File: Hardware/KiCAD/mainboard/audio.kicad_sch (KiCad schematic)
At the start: 16 parts, among them IC1 LM4861M

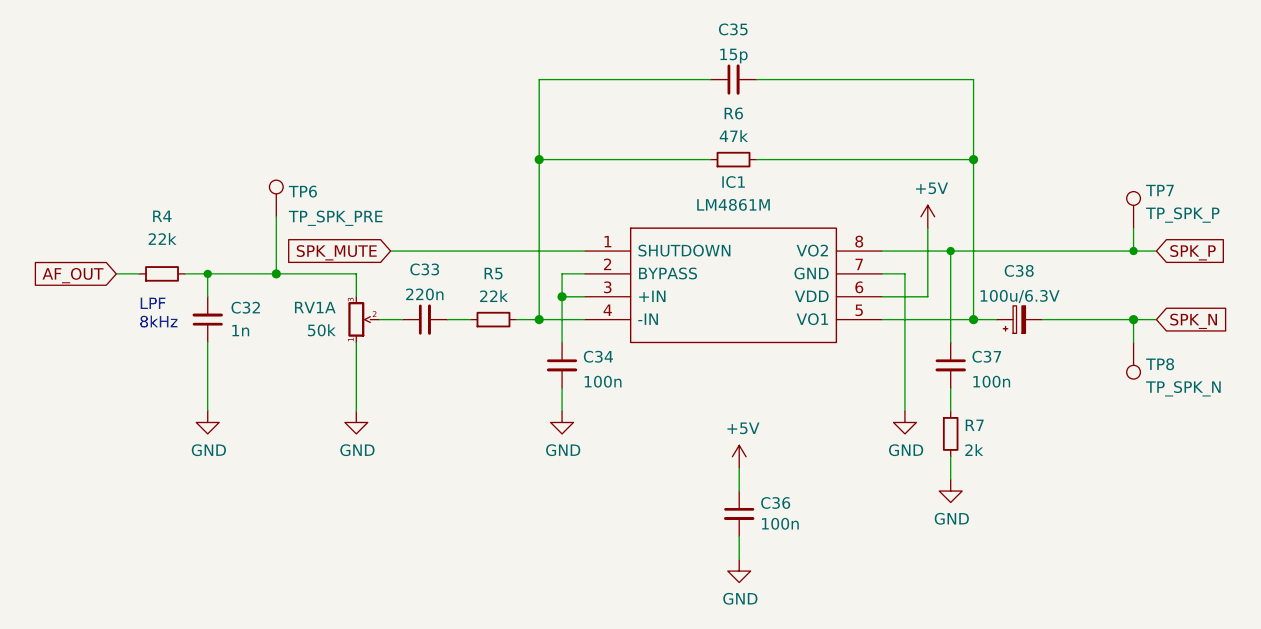
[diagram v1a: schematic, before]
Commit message: MCU swap
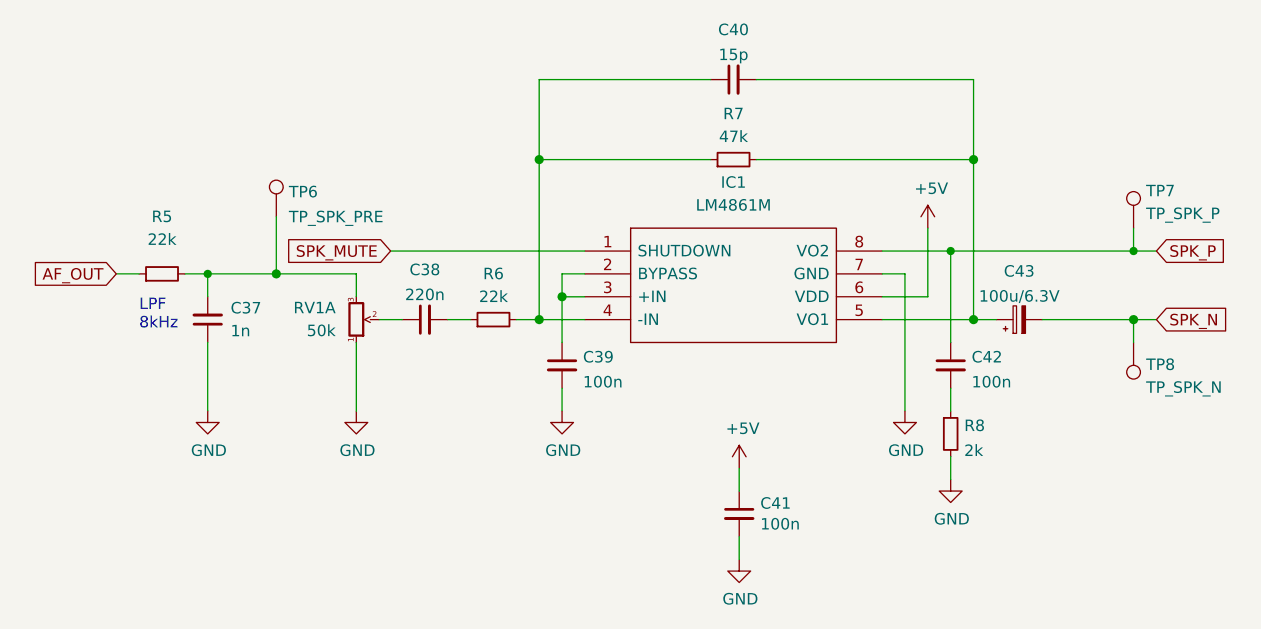
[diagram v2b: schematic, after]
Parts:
- renumbered C32 to C37, C33 to C38, C34 to C39, C35 to C40, C36 to C41, C37 to C42, C38 to C43, R4 to R5, R5 to R6, R6 to R7, R7 to R8
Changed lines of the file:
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@@
   (symbol (lib_id "pkl_device:pkl_R_Small") (at 146.05 84.455 90) (unit 1)
     (in_bom yes) (on_board yes)
-    (property "Reference" "R6" (id 0) (at 146.05 79.375 90))
+    (property "Reference" "R7" (id 0) (at 146.05 79.375 90))
     (property "Value" "47k" (id 1) (at 146.05 81.915 90))
     (property "Footprint" "Resistor_SMD:R_0402_1005Metric" (id 2) (at 146.05 84.455 0)
@@
   (symbol (lib_id "pkl_device:pkl_C_Small") (at 170.18 107.315 0) (unit 1)
     (in_bom yes) (on_board yes) (fields_autoplaced)
-    (property "Reference" "C37" (id 0) (at 172.5042 106.4065 0)
+    (property "Reference" "C42" (id 0) (at 172.5042 106.4065 0)
       (effects (font (size 1.27 1.27)) (justify left))
     )
@@
   (symbol (lib_id "pkl_device:pkl_C_Small") (at 87.63 102.235 180) (unit 1)
     (in_bom yes) (on_board yes) (fields_autoplaced)
-    (property "Reference" "C32" (id 0) (at 90.17 100.9585 0)
+    (property "Reference" "C37" (id 0) (at 90.17 100.9585 0)
       (effects (font (size 1.27 1.27)) (justify right))
     )
@@
   (symbol (lib_id "pkl_device:pkl_C_Small") (at 127 107.315 0) (unit 1)
     (in_bom yes) (on_board yes) (fields_autoplaced)
-    (property "Reference" "C34" (id 0) (at 129.3242 106.4065 0)
+    (property "Reference" "C39" (id 0) (at 129.3242 106.4065 0)
       (effects (font (size 1.27 1.27)) (justify left))
     )
@@
   (symbol (lib_id "pkl_device:pkl_R_Small") (at 119.38 102.235 90) (unit 1)
     (in_bom yes) (on_board yes)
-    (property "Reference" "R5" (id 0) (at 119.38 97.155 90))
+    (property "Reference" "R6" (id 0) (at 119.38 97.155 90))
     (property "Value" "22k" (id 1) (at 119.38 99.695 90))
     (property "Footprint" "Resistor_SMD:R_0402_1005Metric" (id 2) (at 119.38 102.235 0)
@@
   (symbol (lib_id "power:+5V") (at 146.685 118.745 0) (unit 1)
     (in_bom yes) (on_board yes)
-    (property "Reference" "#PWR044" (id 0) (at 146.685 122.555 0)
+    (property "Reference" "#PWR052" (id 0) (at 146.685 122.555 0)
       (effects (font (size 1.27 1.27)) hide)
     )
@@
   (symbol (lib_id "pkl_device:pkl_C_Small") (at 111.76 102.235 90) (unit 1)
     (in_bom yes) (on_board yes) (fields_autoplaced)
-    (property "Reference" "C33" (id 0) (at 111.76 96.7063 90))
+    (property "Reference" "C38" (id 0) (at 111.76 96.7063 90))
     (property "Value" "220n" (id 1) (at 111.76 99.4814 90))
     (property "Footprint" "Capacitor_SMD:C_0402_1005Metric" (id 2) (at 111.76 102.235 0)
@@
   (symbol (lib_id "pkl_device:pkl_C_Small") (at 146.685 123.825 0) (unit 1)
     (in_bom yes) (on_board yes)
-    (property "Reference" "C36" (id 0) (at 149.0218 122.6566 0)
+    (property "Reference" "C41" (id 0) (at 149.0218 122.6566 0)
       (effects (font (size 1.27 1.27)) (justify left))
     )
@@
   (symbol (lib_id "pkl_device:pkl_C_Small") (at 146.05 75.565 90) (unit 1)
     (in_bom yes) (on_board yes) (fields_autoplaced)
-    (property "Reference" "C35" (id 0) (at 146.05 70.0363 90))
+    (property "Reference" "C40" (id 0) (at 146.05 70.0363 90))
     (property "Value" "15p" (id 1) (at 146.05 72.8114 90))
     (property "Footprint" "Capacitor_SMD:C_0402_1005Metric" (id 2) (at 146.05 75.565 0)
@@
   (symbol (lib_id "pkl_device:pkl_R_Small") (at 82.55 97.155 90) (unit 1)
     (in_bom yes) (on_board yes) (fields_autoplaced)
-    (property "Reference" "R4" (id 0) (at 82.55 90.805 90))
+    (property "Reference" "R5" (id 0) (at 82.55 90.805 90))
     (property "Value" "22k" (id 1) (at 82.55 93.345 90))
     (property "Footprint" "Resistor_SMD:R_0402_1005Metric" (id 2) (at 82.55 97.155 0)
@@
   (symbol (lib_id "power:GND") (at 127 112.395 0) (unit 1)
     (in_bom yes) (on_board yes)
-    (property "Reference" "#PWR043" (id 0) (at 127 118.745 0)
+    (property "Reference" "#PWR051" (id 0) (at 127 118.745 0)
       (effects (font (size 1.27 1.27)) hide)
     )
@@
   (symbol (lib_id "power:+5V") (at 167.64 92.075 0) (unit 1)
     (in_bom yes) (on_board yes)
-    (property "Reference" "#PWR047" (id 0) (at 167.64 95.885 0)
+    (property "Reference" "#PWR055" (id 0) (at 167.64 95.885 0)
       (effects (font (size 1.27 1.27)) hide)
     )
@@
   (symbol (lib_id "power:GND") (at 170.18 120.015 0) (unit 1)
     (in_bom yes) (on_board yes)
-    (property "Reference" "#PWR048" (id 0) (at 170.18 126.365 0)
+    (property "Reference" "#PWR056" (id 0) (at 170.18 126.365 0)
       (effects (font (size 1.27 1.27)) hide)
     )
@@
   (symbol (lib_id "power:GND") (at 104.14 112.395 0) (unit 1)
     (in_bom yes) (on_board yes)
-    (property "Reference" "#PWR042" (id 0) (at 104.14 118.745 0)
+    (property "Reference" "#PWR050" (id 0) (at 104.14 118.745 0)
       (effects (font (size 1.27 1.27)) hide)
     )
@@
   (symbol (lib_id "pkl_device:pkl_CP_Small") (at 177.8 102.235 90) (unit 1)
     (in_bom yes) (on_board yes) (fields_autoplaced)
-    (property "Reference" "C38" (id 0) (at 177.8 96.8714 90))
+    (property "Reference" "C43" (id 0) (at 177.8 96.8714 90))
     (property "Value" "100u{slash}6.3V" (id 1) (at 177.8 99.6465 90))
     (property "Footprint" "Capacitor_SMD:C_1206_3216Metric" (id 2) (at 177.8 102.235 0)
@@
   (symbol (lib_id "power:GND") (at 165.1 112.395 0) (unit 1)
     (in_bom yes) (on_board yes)
-    (property "Reference" "#PWR046" (id 0) (at 165.1 118.745 0)
+    (property "Reference" "#PWR054" (id 0) (at 165.1 118.745 0)
       (effects (font (size 1.27 1.27)) hide)
     )
@@
   (symbol (lib_id "power:GND") (at 87.63 112.395 0) (unit 1)
     (in_bom yes) (on_board yes)
-    (property "Reference" "#PWR041" (id 0) (at 87.63 118.745 0)
+    (property "Reference" "#PWR049" (id 0) (at 87.63 118.745 0)
       (effects (font (size 1.27 1.27)) hide)
     )
@@
   (symbol (lib_id "pkl_device:pkl_R_Small") (at 170.18 114.935 0) (unit 1)
     (in_bom yes) (on_board yes) (fields_autoplaced)
-    (property "Reference" "R7" (id 0) (at 171.6787 114.0265 0)
+    (property "Reference" "R8" (id 0) (at 171.6787 114.0265 0)
       (effects (font (size 1.27 1.27)) (justify left))
     )
@@
   (symbol (lib_id "power:GND") (at 146.685 128.905 0) (unit 1)
     (in_bom yes) (on_board yes)
-    (property "Reference" "#PWR045" (id 0) (at 146.685 135.255 0)
-      (effects (font (size 1.27 1.27)) hide)
-    )
+    (property "Reference" "#PWR053" (id 0) (at 146.685 135.255 0)
+      (effects (font (size 1.27 1.27)) hide)
+    )

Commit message: Removed RTC
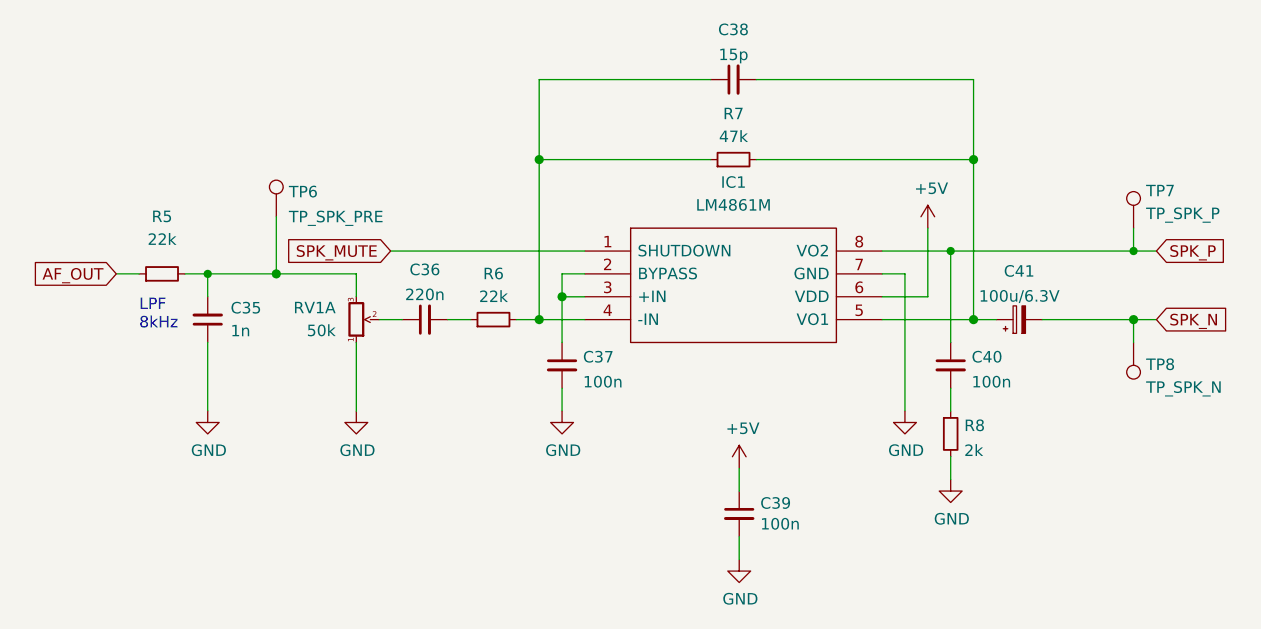
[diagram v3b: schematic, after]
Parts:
- renumbered C37 to C35, C38 to C36, C39 to C37, C40 to C38, C41 to C39, C42 to C40, C43 to C41
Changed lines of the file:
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@@
   (symbol (lib_id "pkl_device:pkl_C_Small") (at 170.18 107.315 0) (unit 1)
     (in_bom yes) (on_board yes) (fields_autoplaced)
-    (property "Reference" "C42" (id 0) (at 172.5042 106.4065 0)
+    (property "Reference" "C40" (id 0) (at 172.5042 106.4065 0)
       (effects (font (size 1.27 1.27)) (justify left))
     )
@@
   (symbol (lib_id "pkl_device:pkl_C_Small") (at 87.63 102.235 180) (unit 1)
     (in_bom yes) (on_board yes) (fields_autoplaced)
-    (property "Reference" "C37" (id 0) (at 90.17 100.9585 0)
+    (property "Reference" "C35" (id 0) (at 90.17 100.9585 0)
       (effects (font (size 1.27 1.27)) (justify right))
     )
@@
   (symbol (lib_id "pkl_device:pkl_C_Small") (at 127 107.315 0) (unit 1)
     (in_bom yes) (on_board yes) (fields_autoplaced)
-    (property "Reference" "C39" (id 0) (at 129.3242 106.4065 0)
+    (property "Reference" "C37" (id 0) (at 129.3242 106.4065 0)
       (effects (font (size 1.27 1.27)) (justify left))
     )
@@
   (symbol (lib_id "power:+5V") (at 146.685 118.745 0) (unit 1)
     (in_bom yes) (on_board yes)
-    (property "Reference" "#PWR052" (id 0) (at 146.685 122.555 0)
+    (property "Reference" "#PWR050" (id 0) (at 146.685 122.555 0)
       (effects (font (size 1.27 1.27)) hide)
     )
@@
   (symbol (lib_id "pkl_device:pkl_C_Small") (at 111.76 102.235 90) (unit 1)
     (in_bom yes) (on_board yes) (fields_autoplaced)
-    (property "Reference" "C38" (id 0) (at 111.76 96.7063 90))
+    (property "Reference" "C36" (id 0) (at 111.76 96.7063 90))
     (property "Value" "220n" (id 1) (at 111.76 99.4814 90))
     (property "Footprint" "Capacitor_SMD:C_0402_1005Metric" (id 2) (at 111.76 102.235 0)
@@
   (symbol (lib_id "pkl_device:pkl_C_Small") (at 146.685 123.825 0) (unit 1)
     (in_bom yes) (on_board yes)
-    (property "Reference" "C41" (id 0) (at 149.0218 122.6566 0)
+    (property "Reference" "C39" (id 0) (at 149.0218 122.6566 0)
       (effects (font (size 1.27 1.27)) (justify left))
     )
@@
   (symbol (lib_id "pkl_device:pkl_C_Small") (at 146.05 75.565 90) (unit 1)
     (in_bom yes) (on_board yes) (fields_autoplaced)
-    (property "Reference" "C40" (id 0) (at 146.05 70.0363 90))
+    (property "Reference" "C38" (id 0) (at 146.05 70.0363 90))
     (property "Value" "15p" (id 1) (at 146.05 72.8114 90))
     (property "Footprint" "Capacitor_SMD:C_0402_1005Metric" (id 2) (at 146.05 75.565 0)
@@
   (symbol (lib_id "power:GND") (at 127 112.395 0) (unit 1)
     (in_bom yes) (on_board yes)
-    (property "Reference" "#PWR051" (id 0) (at 127 118.745 0)
+    (property "Reference" "#PWR049" (id 0) (at 127 118.745 0)
       (effects (font (size 1.27 1.27)) hide)
     )
@@
   (symbol (lib_id "power:+5V") (at 167.64 92.075 0) (unit 1)
     (in_bom yes) (on_board yes)
-    (property "Reference" "#PWR055" (id 0) (at 167.64 95.885 0)
+    (property "Reference" "#PWR053" (id 0) (at 167.64 95.885 0)
       (effects (font (size 1.27 1.27)) hide)
     )
@@
   (symbol (lib_id "power:GND") (at 170.18 120.015 0) (unit 1)
     (in_bom yes) (on_board yes)
-    (property "Reference" "#PWR056" (id 0) (at 170.18 126.365 0)
+    (property "Reference" "#PWR054" (id 0) (at 170.18 126.365 0)
       (effects (font (size 1.27 1.27)) hide)
     )
@@
   (symbol (lib_id "power:GND") (at 104.14 112.395 0) (unit 1)
     (in_bom yes) (on_board yes)
-    (property "Reference" "#PWR050" (id 0) (at 104.14 118.745 0)
+    (property "Reference" "#PWR048" (id 0) (at 104.14 118.745 0)
       (effects (font (size 1.27 1.27)) hide)
     )
@@
   (symbol (lib_id "pkl_device:pkl_CP_Small") (at 177.8 102.235 90) (unit 1)
     (in_bom yes) (on_board yes) (fields_autoplaced)
-    (property "Reference" "C43" (id 0) (at 177.8 96.8714 90))
+    (property "Reference" "C41" (id 0) (at 177.8 96.8714 90))
     (property "Value" "100u{slash}6.3V" (id 1) (at 177.8 99.6465 90))
     (property "Footprint" "Capacitor_SMD:C_1206_3216Metric" (id 2) (at 177.8 102.235 0)
@@
   (symbol (lib_id "power:GND") (at 165.1 112.395 0) (unit 1)
     (in_bom yes) (on_board yes)
-    (property "Reference" "#PWR054" (id 0) (at 165.1 118.745 0)
+    (property "Reference" "#PWR052" (id 0) (at 165.1 118.745 0)
       (effects (font (size 1.27 1.27)) hide)
     )
@@
   (symbol (lib_id "power:GND") (at 87.63 112.395 0) (unit 1)
     (in_bom yes) (on_board yes)
-    (property "Reference" "#PWR049" (id 0) (at 87.63 118.745 0)
+    (property "Reference" "#PWR047" (id 0) (at 87.63 118.745 0)
       (effects (font (size 1.27 1.27)) hide)
     )
@@
   (symbol (lib_id "power:GND") (at 146.685 128.905 0) (unit 1)
     (in_bom yes) (on_board yes)
-    (property "Reference" "#PWR053" (id 0) (at 146.685 135.255 0)
-      (effects (font (size 1.27 1.27)) hide)
-    )
+    (property "Reference" "#PWR051" (id 0) (at 146.685 135.255 0)
+      (effects (font (size 1.27 1.27)) hide)
+    )
